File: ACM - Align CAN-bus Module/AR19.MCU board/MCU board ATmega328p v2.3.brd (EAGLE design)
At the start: 19 x 26.3 mm, 36 parts, among them IC1 ATMEGA328P-MMH, IC2 MIC5239-5.0YS_TR, IC3 MCP25625-E_ML, J1 AVR_SPI_PROG_3X2NS

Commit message: Oppdatering MCP-25625
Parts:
- added C10, C9: 22pF, 12066D106KAT2A:CAPC3216X229N
- added QF2: 16M20AUM1, crystal:UM1
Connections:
- removed net N$7: IC1.28
- removed net OSC1: C2.2, IC1.5, IC3.21, QF1.1
- removed net OSC2: C3.2, IC1.6, IC3.20, QF1.3
- new net CAN_OSC1: C9.2, IC3.21, QF2.1
- new net CAN_OSC2: C10.2, IC3.20, QF2.3
- new net MCU_OSC1: C2.2, IC1.5, QF1.1
- new net MCU_OSC2: C3.2, IC1.6, QF1.3
- net CAN_INIT: now also IC1.28
- net GND: now also C10.1, C9.1, QF2.2
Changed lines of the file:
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@@
 <attribute name="VALUE" x="-8.89" y="-38.735" size="1.27" layer="27"/>
+</element>
+<element name="C9" library="12066D106KAT2A" package="CAPC3216X229N" value="22pF" x="-6.985" y="-48.26">
+<attribute name="ALLIED_NUMBER" value="70002294" x="-5.715" y="-40.64" size="1.778" layer="27" display="off"/>
+<attribute name="ALLIED_PRICE-STOCK" value="http://www.alliedelec.com/avx-12066d106kat2a/70002294/" x="-5.715" y="-40.64" size="1.778" layer="27" display="off"/>
+<attribute name="ARROW_PART_NUMBER" value="12066D106KAT2A" x="-5.715" y="-40.64" size="1.778" layer="27" display="off"/>
+<attribute name="ARROW_PRICE-STOCK" value="http://uk.rs-online.com/web/p/products/1356756" x="-5.715" y="-40.64" size="1.778" layer="27" display="off"/>
+<attribute name="DESCRIPTION" value="AVX 10uF  /-10% 6.3 V dc X5R Dielectric SMD Ceramic Multilayer Capacitor 1206" x="-5.715" y="-40.64" size="1.778" layer="27" display="off"/>
+<attribute name="HEIGHT" value="2.29mm" x="-5.715" y="-40.64" size="1.778" layer="27" display="off"/>
+<attribute name="MANUFACTURER_NAME" value="AVX" x="-5.715" y="-40.64" size="1.778" layer="27" display="off"/>
+<attribute name="MANUFACTURER_PART_NUMBER" value="12066D106KAT2A" x="-5.715" y="-40.64" size="1.778" layer="27" display="off"/>
+<attribute name="NAME" x="-5.715" y="-40.64" size="1.27" layer="25" align="center"/>
+<attribute name="RS_PART_NUMBER" value="1356756" x="-5.715" y="-40.64" size="1.778" layer="27" display="off"/>
+<attribute name="RS_PRICE-STOCK" value="http://uk.rs-online.com/web/p/products/1356756" x="-5.715" y="-40.64" size="1.778" layer="27" display="off"/>
+<attribute name="VALUE" x="-5.715" y="-40.64" size="1.27" layer="27" align="center"/>
+</element>
+<element name="C10" library="12066D106KAT2A" package="CAPC3216X229N" value="22pF" x="-1.905" y="-48.26">
+<attribute name="ALLIED_NUMBER" value="70002294" x="-5.715" y="-43.18" size="1.778" layer="27" display="off"/>
+<attribute name="ALLIED_PRICE-STOCK" value="http://www.alliedelec.com/avx-12066d106kat2a/70002294/" x="-5.715" y="-43.18" size="1.778" layer="27" display="off"/>
+<attribute name="ARROW_PART_NUMBER" value="12066D106KAT2A" x="-5.715" y="-43.18" size="1.778" layer="27" display="off"/>
+<attribute name="ARROW_PRICE-STOCK" value="http://uk.rs-online.com/web/p/products/1356756" x="-5.715" y="-43.18" size="1.778" layer="27" display="off"/>
+<attribute name="DESCRIPTION" value="AVX 10uF  /-10% 6.3 V dc X5R Dielectric SMD Ceramic Multilayer Capacitor 1206" x="-5.715" y="-43.18" size="1.778" layer="27" display="off"/>
+<attribute name="HEIGHT" value="2.29mm" x="-5.715" y="-43.18" size="1.778" layer="27" display="off"/>
+<attribute name="MANUFACTURER_NAME" value="AVX" x="-5.715" y="-43.18" size="1.778" layer="27" display="off"/>
+<attribute name="MANUFACTURER_PART_NUMBER" value="12066D106KAT2A" x="-5.715" y="-43.18" size="1.778" layer="27" display="off"/>
+<attribute name="NAME" x="-5.715" y="-43.18" size="1.27" layer="25" align="center"/>
+<attribute name="RS_PART_NUMBER" value="1356756" x="-5.715" y="-43.18" size="1.778" layer="27" display="off"/>
+<attribute name="RS_PRICE-STOCK" value="http://uk.rs-online.com/web/p/products/1356756" x="-5.715" y="-43.18" size="1.778" layer="27" display="off"/>
+<attribute name="VALUE" x="-5.715" y="-43.18" size="1.27" layer="27" align="center"/>
+</element>
+<element name="QF2" library="crystal" library_urn="urn:adsk.eagle:library:204" package="UM1" package3d_urn="urn:adsk.eagle:package:12117/1" value="16M20AUM1" x="-5.08" y="-43.18">
+<attribute name="MF" value="" x="-5.08" y="-48.26" size="1.778" layer="27" display="off"/>
+<attribute name="MPN" value="" x="-5.08" y="-48.26" size="1.778" layer="27" display="off"/>
+<attribute name="NAME" x="-8.89" y="-46.355" size="1.27" layer="25" ratio="10"/>
+<attribute name="OC_FARNELL" value="unknown" x="-5.08" y="-48.26" size="1.778" layer="27" display="off"/>
+<attribute name="OC_NEWARK" value="unknown" x="-5.08" y="-48.26" size="1.778" layer="27" display="off"/>
+<attribute name="VALUE" x="-8.89" y="-51.435" size="1.27" layer="27" ratio="10"/>
 </element>
 </elements>
@@
 <contactref element="C2" pad="1"/>
 <contactref element="C3" pad="1"/>
+<contactref element="QF2" pad="2"/>
+<contactref element="C9" pad="1"/>
+<contactref element="C10" pad="1"/>
+<wire x1="-3.305" y1="-48.26" x2="-8.385" y2="-48.26" width="0" layer="19" extent="1-1"/>
+<wire x1="-5.107" y1="-43.18" x2="-3.305" y2="-48.26" width="0" layer="19" extent="1-1"/>
+<wire x1="-7.405" y1="-36.83" x2="-5.107" y2="-43.18" width="0" layer="19" extent="1-1"/>
 <wire x1="-7.405" y1="-31.75" x2="-7.405" y2="-36.83" width="0" layer="19" extent="1-1"/>
 <wire x1="-7.405" y1="-26.67" x2="-7.405" y2="-31.75" width="0" layer="19" extent="1-1"/>
@@
 <contactref element="IC3" pad="27"/>
 </signal>
-<signal name="OSC1">
-<contactref element="IC3" pad="21"/>
-<contactref element="C2" pad="2"/>
-<contactref element="IC1" pad="5"/>
-<contactref element="QF1" pad="1"/>
-<wire x1="7.93" y1="15.92" x2="11.935" y2="21.59" width="0" layer="19" extent="1-1"/>
-<wire x1="11.285" y1="10.98" x2="7.93" y2="15.92" width="0" layer="19" extent="1-1"/>
-<wire x1="-6.955" y1="-3.81" x2="11.285" y2="10.98" width="0" layer="19" extent="1-1"/>
-</signal>
-<signal name="OSC2">
-<contactref element="IC3" pad="20"/>
-<contactref element="C3" pad="2"/>
-<contactref element="IC1" pad="6"/>
-<contactref element="QF1" pad="3"/>
-<wire x1="7.93" y1="15.27" x2="14.735" y2="24.13" width="0" layer="19" extent="1-1"/>
-<wire x1="11.285" y1="10.53" x2="7.93" y2="15.27" width="0" layer="19" extent="1-1"/>
-<wire x1="-3.205" y1="-3.81" x2="11.285" y2="10.53" width="0" layer="19" extent="1-1"/>
-</signal>
 <signal name="TXCAN">
 <contactref element="IC3" pad="4"/>
@@
 <contactref element="IC1" pad="12"/>
 </signal>
-<signal name="N$7">
-<contactref element="IC1" pad="28"/>
-</signal>
 <signal name="N$8">
 <contactref element="IC1" pad="27"/>
@@
 <signal name="CAN_INIT">
 <contactref element="IC3" pad="25"/>
+<contactref element="IC1" pad="28"/>
+<wire x1="5.08" y1="16.82" x2="11.985" y2="13.48" width="0" layer="19" extent="1-1"/>
 </signal>
 <signal name="N$1">
@@
 <wire x1="2.23" y1="15.27" x2="-9.105" y2="-19.05" width="0" layer="19" extent="1-1"/>
 </signal>
+<signal name="MCU_OSC1">
+<contactref element="IC1" pad="5"/>
+<contactref element="C2" pad="2"/>
+<contactref element="QF1" pad="1"/>
+<wire x1="11.285" y1="10.98" x2="11.935" y2="21.59" width="0" layer="19" extent="1-1"/>
+<wire x1="-6.955" y1="-3.81" x2="11.285" y2="10.98" width="0" layer="19" extent="1-1"/>
+</signal>
+<signal name="MCU_OSC2">
+<contactref element="IC1" pad="6"/>
+<contactref element="C3" pad="2"/>
+<contactref element="QF1" pad="3"/>
+<wire x1="11.285" y1="10.53" x2="14.735" y2="24.13" width="0" layer="19" extent="1-1"/>
+<wire x1="-3.205" y1="-3.81" x2="11.285" y2="10.53" width="0" layer="19" extent="1-1"/>
+</signal>
+<signal name="CAN_OSC1">
+<contactref element="IC3" pad="21"/>
+<contactref element="C9" pad="2"/>
+<contactref element="QF2" pad="1"/>
+<wire x1="-6.955" y1="-43.18" x2="-5.585" y2="-48.26" width="0" layer="19" extent="1-1"/>
+<wire x1="7.93" y1="15.92" x2="-6.955" y2="-43.18" width="0" layer="19" extent="1-1"/>
+</signal>
+<signal name="CAN_OSC2">
+<contactref element="IC3" pad="20"/>
+<contactref element="C10" pad="2"/>
+<contactref element="QF2" pad="3"/>
+<wire x1="-3.205" y1="-43.18" x2="-0.505" y2="-48.26" width="0" layer="19" extent="1-1"/>
+<wire x1="7.93" y1="15.27" x2="-3.205" y2="-43.18" width="0" layer="19" extent="1-1"/>
+</signal>
 </signals>

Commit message: Ryddet og la til den nye krystallen
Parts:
- removed QF1, QF2: 16M20AUM1, crystal:UM1
- added U$1, U$2: FA-20H, FA-20H 16.0000MF20X-B:FA-20H
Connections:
- net CAN_OSC1: now also U$1.1; no longer QF2.1
- net CAN_OSC2: now also U$1.3; no longer QF2.3
- net GND: no longer QF1.2, QF2.2
- net MCU_OSC1: now also U$2.1; no longer QF1.1
- net MCU_OSC2: now also U$2.3; no longer QF1.3

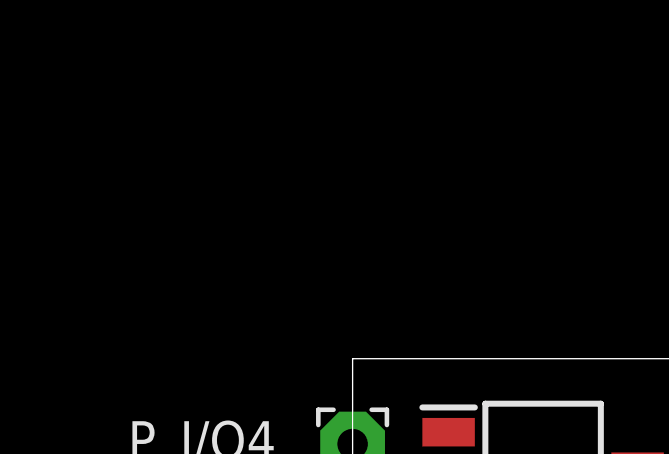
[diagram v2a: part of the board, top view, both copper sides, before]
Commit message: Added: Fuse Block (Littelfuse SMD fuse block)
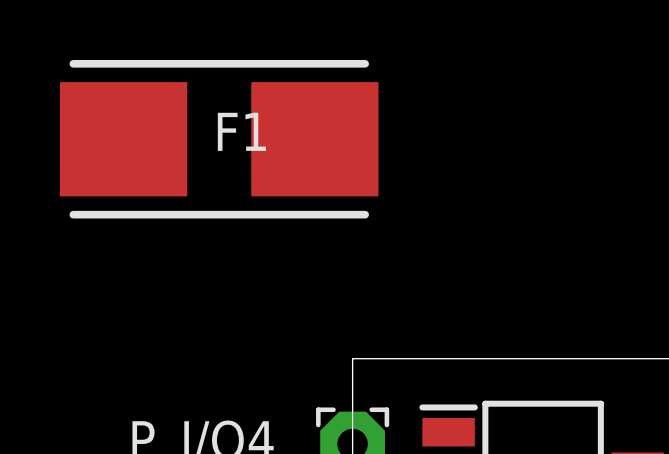
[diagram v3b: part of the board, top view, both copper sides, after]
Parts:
- added F1: 0154005.DRT, 0154005(Fuseholder)DRT:0154001.DRT
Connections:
- new net N$2: C4.2, F1.2, IC2.1
- net VCC: now also F1.1; no longer C4.2, IC2.1
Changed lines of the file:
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@@
 <element name="U$1" library="FA-20H 16.0000MF20X-B" package="FA-20H" value="FA-20H" x="-8.89" y="-52.705" smashed="yes"/>
 <element name="U$2" library="FA-20H 16.0000MF20X-B" package="FA-20H" value="FA-20H" x="-8.89" y="-57.15" smashed="yes"/>
+<element name="F1" library="0154005(Fuseholder)DRT" package="0154001.DRT" value="0154005.DRT" x="-5.08" y="33.655" smashed="yes" rot="R180">
+<attribute name="ALLIED_NUMBER" value="70184875" x="-5.08" y="33.655" size="1.778" layer="27" rot="R180" display="off"/>
+<attribute name="ALLIED_PRICE-STOCK" value="https://www.alliedelec.com/littelfuse-0154005-drt/70184875/" x="-5.08" y="33.655" size="1.778" layer="27" rot="R180" display="off"/>
+<attribute name="ARROW_PART_NUMBER" value="0154005.DRT" x="-5.08" y="33.655" size="1.778" layer="27" rot="R180" display="off"/>
+<attribute name="ARROW_PRICE-STOCK" value="https://www.arrow.com/en/products/0154005.drt/littelfuse" x="-5.08" y="33.655" size="1.778" layer="27" rot="R180" display="off"/>
+<attribute name="DESCRIPTION" value="Littelfuse 5A T Surface Mount Fuse, 125V ac/dc" x="-5.08" y="33.655" size="1.778" layer="27" rot="R180" display="off"/>
+<attribute name="HEIGHT" value="mm" x="-5.08" y="33.655" size="1.778" layer="27" rot="R180" display="off"/>
+<attribute name="MANUFACTURER_NAME" value="LITTELFUSE" x="-5.08" y="33.655" size="1.778" layer="27" rot="R180" display="off"/>
+<attribute name="MANUFACTURER_PART_NUMBER" value="0154005.DRT" x="-5.08" y="33.655" size="1.778" layer="27" rot="R180" display="off"/>
+<attribute name="NAME" x="-4.3313" y="33.902" size="1.27" layer="25" rot="R180" align="center"/>
+<attribute name="RS_PART_NUMBER" value="2196260P" x="-5.08" y="33.655" size="1.778" layer="27" rot="R180" display="off"/>
+<attribute name="RS_PRICE-STOCK" value="http://uk.rs-online.com/web/p/products/2196260P" x="-5.08" y="33.655" size="1.778" layer="27" rot="R180" display="off"/>
+<attribute name="VALUE" x="-4.3313" y="33.902" size="1.27" layer="27" rot="R180" align="center"/>
+</element>
 </elements>
 <signals>
@@
 <signal name="VCC">
 <contactref element="P_VCC" pad="1"/>
-<contactref element="C4" pad="2"/>
-<contactref element="IC2" pad="1"/>
-<wire x1="-0.635" y1="10.795" x2="2.565" y2="23.89" width="0" layer="19" extent="1-1"/>
-<wire x1="12.7" y1="4.525" x2="-0.635" y2="10.795" width="0" layer="19" extent="1-1"/>
+<contactref element="F1" pad="1"/>
+<wire x1="-0.635" y1="10.795" x2="-1.8923" y2="33.655" width="0" layer="19" extent="1-1"/>
 </signal>
 <signal name="CANL">
@@
 <wire x1="7.93" y1="15.27" x2="-0.505" y2="-48.26" width="0" layer="19" extent="1-1"/>
 </signal>
+<signal name="N$2">
+<contactref element="F1" pad="2"/>
+<contactref element="C4" pad="2"/>
+<contactref element="IC2" pad="1"/>
+<wire x1="2.565" y1="23.89" x2="-8.2677" y2="33.655" width="0" layer="19" extent="1-1"/>
+<wire x1="12.7" y1="4.525" x2="2.565" y2="23.89" width="0" layer="19" extent="1-1"/>
+</signal>
 </signals>

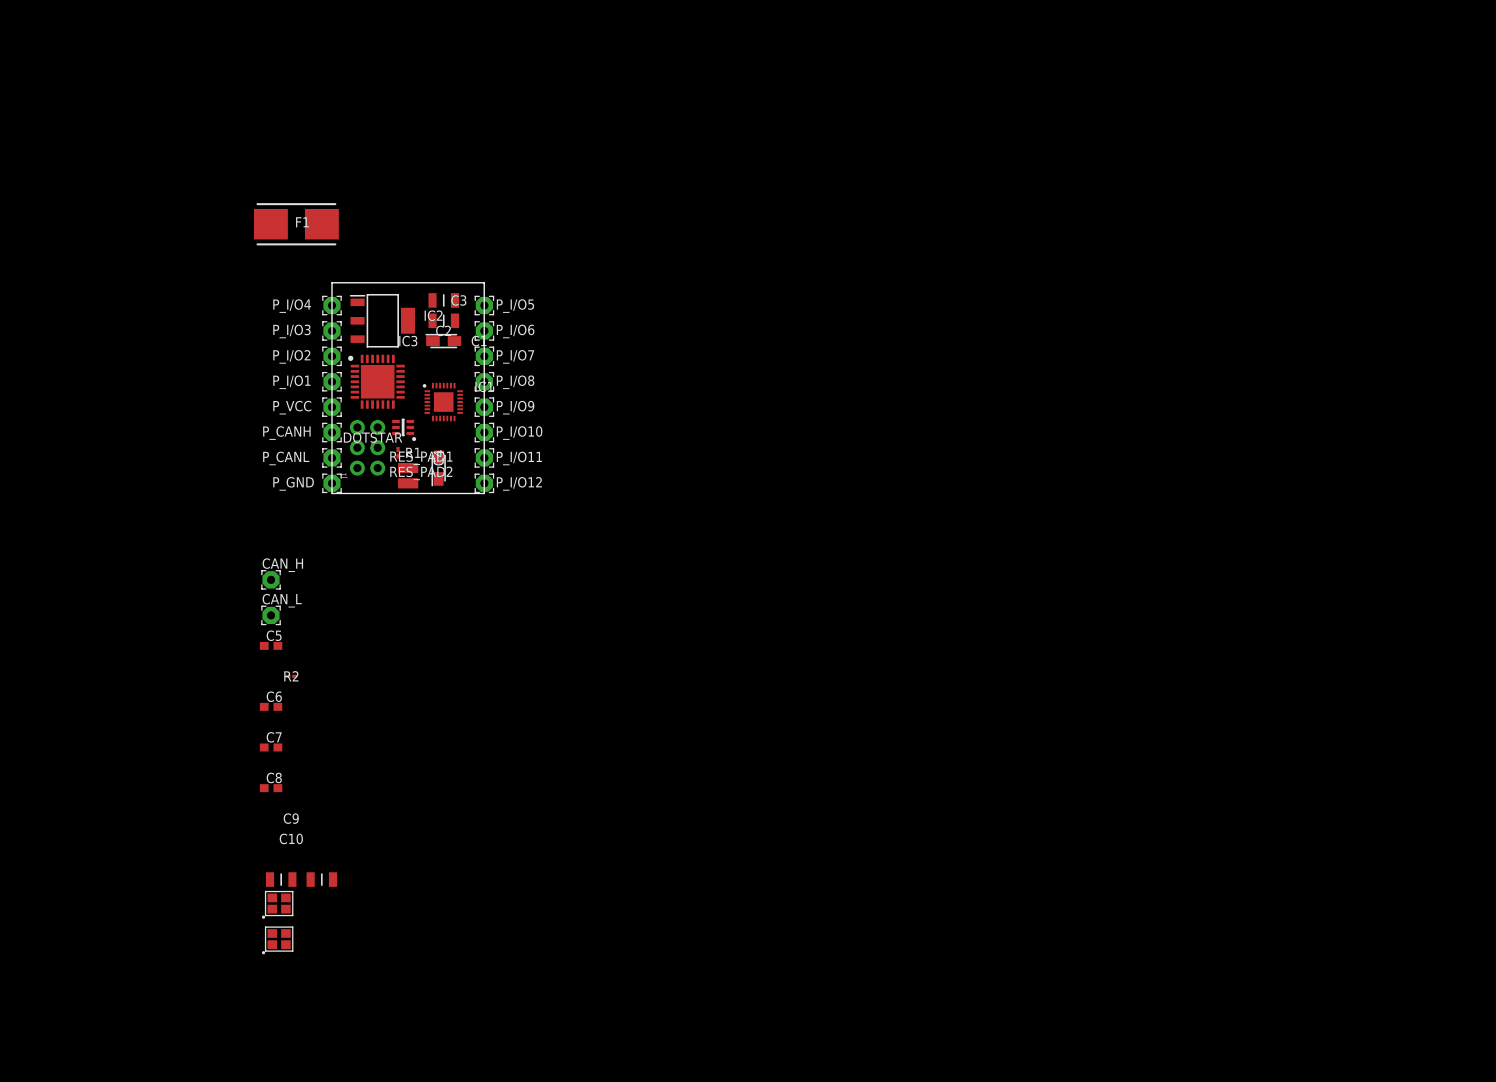
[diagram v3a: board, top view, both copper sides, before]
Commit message: Exploded PCB Board
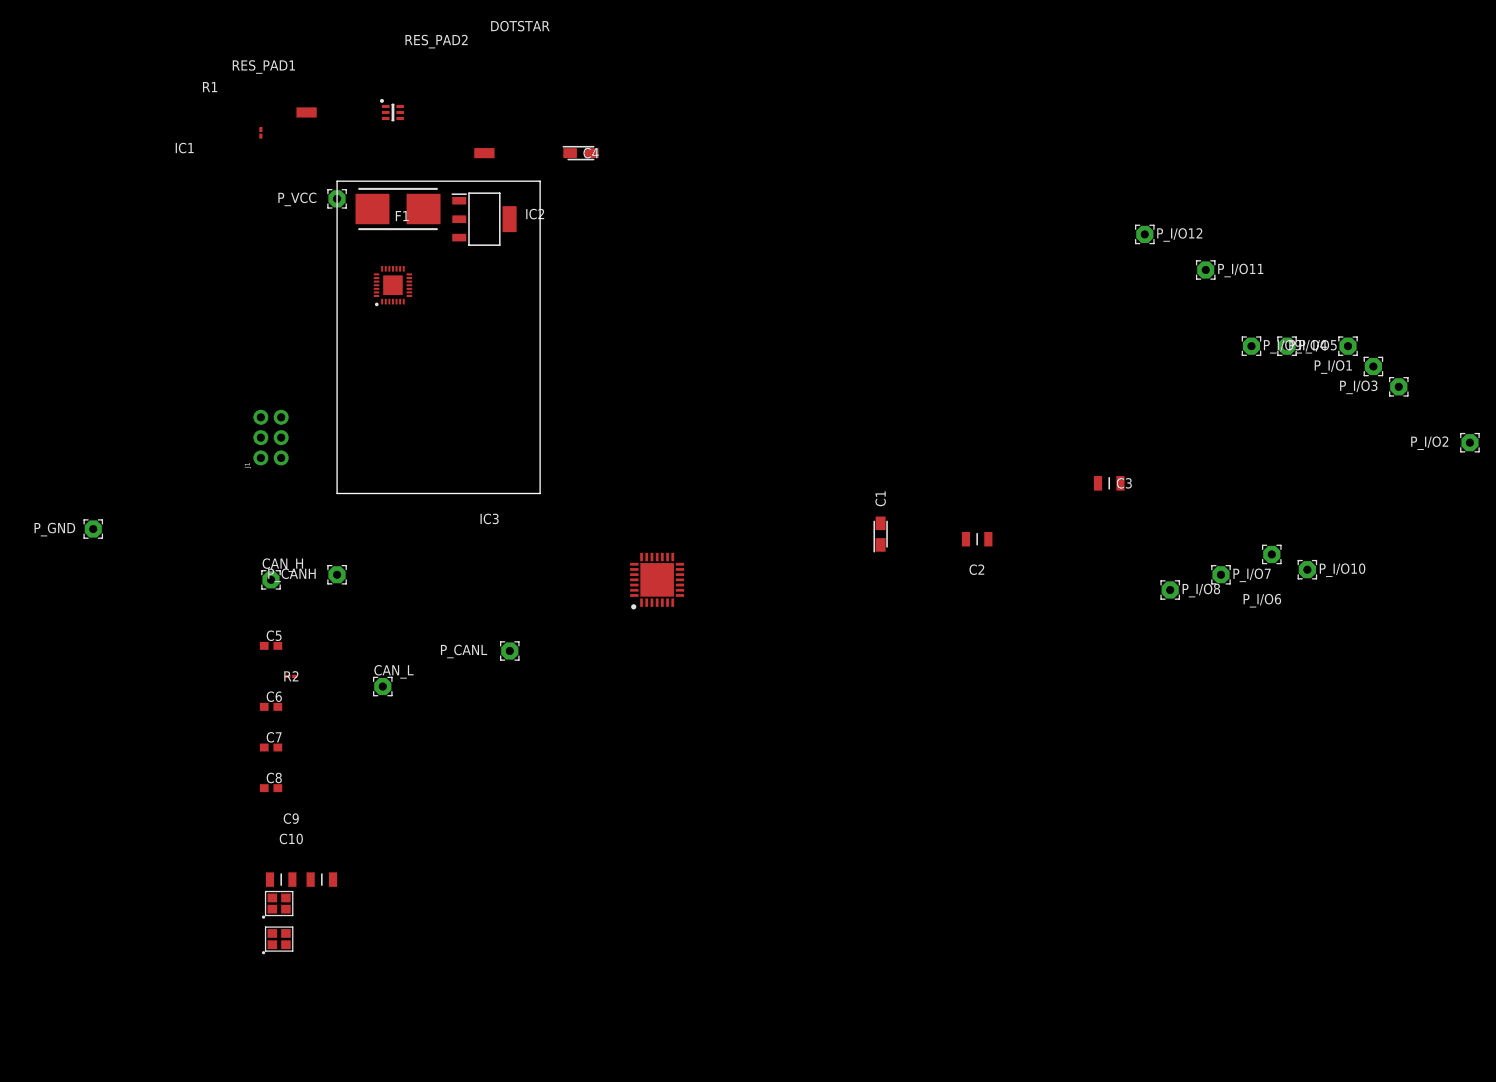
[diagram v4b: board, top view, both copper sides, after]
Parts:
- moved P_I/O2 142.6 mm to (141.6, 6.35)
- moved P_I/O3 133.5 mm to (132.7, 13.3)
- moved P_I/O1 130.2 mm to (129.5, 15.9)
- moved P_I/O4 127.1 mm to (126.4, 18.4)
- moved P_I/O10 104.3 mm to (121.3, -9.53)
- moved P_I/O6 102.3 mm to (116.8, -7.62)
- moved P_I/O5 100.5 mm to (118.7, 18.4)
- moved P_I/O9 96.2 mm to (114.3, 18.4)
- moved P_I/O7 96.0 mm to (110.5, -10.2)
- moved P_I/O11 93.2 mm to (108.6, 27.9)
- moved P_I/O8 89.6 mm to (104.1, -12.1)
- moved P_I/O12 88.2 mm to (101.0, 32.4)
- moved C3 86.3 mm to (96.5, 1.27)
- moved C2 72.0 mm to (80.0, -5.71)
- moved C1 59.7 mm to (67.9, -5.08), turned to 90 degrees
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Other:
- board size 19 x 26.3 mm -> 25.4 x 39 mm
